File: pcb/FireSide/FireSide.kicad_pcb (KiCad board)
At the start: 2 copper layers, 120 x 80 mm, 27 parts, among them J0 SDIOModule, J1 D4184_PIN_A, J10 5V_01x02_JST, J11 5V_01x02_JST, J12 Status_01x02_JST, J2 D4184_PIN_B, J3 D4184_PIN_C, J4 A0_01x02_JST, J5 A1_01x02_JST, J6 A2_01x02_JST, J60 XT60-Male, J7 A3_01x02_JST, J8 A4_01x02_JST, J9 A5_01x02_JST, Q1 MMBT2222A, U1 AMS1117-5.0, U3 RYLR998

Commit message: [FS] PCB Updated to v1.1.6
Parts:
- removed A1: Nucleo-L412KB, Module:Arduino_Nano
- removed H5, H6: BoardM4, MountingHole:MountingHole_4.3mm_M4_ISO7380_Pad_TopBottom
- removed J0: SDIOModule, Connector_Molex:Molex_Nano-Fit_105309-xx08_1x08_P2.50mm_Vertical
- removed J60: XT60-Male, XT60-M:AMASS_XT60-M
- removed R1: 1k, Resistor_SMD:R_0805_2012Metric_Pad1.20x1.40mm_HandSolder
- added C3: 10uF, Capacitor_SMD:C_0805_2012Metric, F.Cu at (107.0, 46.8)
- added C4: 22uF, Capacitor_SMD:C_0805_2012Metric, F.Cu at (90.8, 50.5)
- added C5: 100nF, Capacitor_SMD:C_0805_2012Metric, F.Cu at (130.9, 67.6)
- added C6: 4.7uF, Capacitor_SMD:C_0805_2012Metric, F.Cu at (130.9, 71.0)
- added G***: LOGO, logos:logo2, F.Cu at (106.1, 64.4)
- added J13: Screw_Terminal_01x03, TerminalBlock:TerminalBlock_bornier-3_P5.08mm, F.Cu at (139.8, 52.9)
- added J14: Conn_01x02_Pin, Connector_JST:JST_XH_B2B-XH-A_1x02_P2.50mm_Vertical, F.Cu at (142.8, 65.2)
- added R2: 100k, Resistor_THT:R_Axial_DIN0204_L3.6mm_D1.6mm_P5.08mm_Horizontal, F.Cu at (147.8, 109.5)
- added R4: 1k, Resistor_SMD:R_0805_2012Metric, F.Cu at (128.2, 54.0)
- added R5: 100k, Resistor_THT:R_Axial_DIN0204_L3.6mm_D1.6mm_P5.08mm_Horizontal, F.Cu at (147.8, 96.5)
- added R6: 100k, Resistor_THT:R_Axial_DIN0204_L3.6mm_D1.6mm_P5.08mm_Horizontal, F.Cu at (147.8, 83.5)
- added R7: 100k, Resistor_THT:R_Axial_DIN0204_L3.6mm_D1.6mm_P5.08mm_Horizontal, F.Cu at (147.8, 70.5)
- added TP1: TestPoint, TestPoint:TestPoint_Loop_D2.60mm_Drill1.6mm_Beaded, F.Cu at (126.5, 48.5)
- added TP2: TestPoint, TestPoint:TestPoint_Loop_D2.60mm_Drill1.6mm_Beaded, F.Cu at (95.2, 42.2)
- added U2: ~, FireSide Footprint:RYLR998, F.Cu at (78.7, 67.3)
- added U4: AMS1117-5.0, Package_TO_SOT_SMD:SOT-223-3_TabPin2, F.Cu at (113.0, 50.9)
- added U5: ~, FireSide Footprint:D4184, F.Cu at (95.0, 85.8)
- added U6: ~, FireSide Footprint:D4184, F.Cu at (95.0, 121.0)
- added U8: ~, FireSide Footprint:XT60-M, F.Cu at (107.6, 29.6)
- added U9: ~, FireSide Footprint:D4184, F.Cu at (95.0, 103.2)
- C1: value 22u -> 22uF; footprint Capacitor_THT:CP_Radial_D5.0mm_P2.50mm -> Capacitor_SMD:C_0805_2012Metric
- C2: value 22u -> 10uF; footprint Capacitor_THT:CP_Radial_D5.0mm_P2.50mm -> Capacitor_SMD:C_0805_2012Metric
- H1, H2: value SDModuleM3 -> MountingHole_Pad; footprint MountingHole:MountingHole_3.2mm_M3_ISO7380_Pad_TopBottom -> MountingHole:MountingHole_4.3mm_M4_DIN965_Pad
- H3, H4: value BoardM4 -> MountingHole_Pad; footprint MountingHole:MountingHole_4.3mm_M4_ISO7380_Pad_TopBottom -> MountingHole:MountingHole_4.3mm_M4_DIN965_Pad
- J1: value D4184_PIN_A -> Conn_01x02_Pin; footprint Connector_JST:JST_XH_B4B-XH-A_1x04_P2.50mm_Vertical -> Connector_JST:JST_XH_B2B-XH-A_1x02_P2.50mm_Vertical
- J10, J11: value 5V_01x02_JST -> Conn_01x02_Pin
- J12: value Status_01x02_JST -> Conn_01x02_Pin
- J2: value D4184_PIN_B -> Conn_01x02_Pin; footprint Connector_JST:JST_XH_B4B-XH-A_1x04_P2.50mm_Vertical -> Connector_JST:JST_XH_B2B-XH-A_1x02_P2.50mm_Vertical
- J3: value D4184_PIN_C -> Conn_01x08_Pin; footprint Connector_JST:JST_XH_B4B-XH-A_1x04_P2.50mm_Vertical -> Connector_PinHeader_2.54mm:PinHeader_1x08_P2.54mm_Vertical
- J4: value A0_01x02_JST -> Conn_01x02_Pin
- J5: value A1_01x02_JST -> Conn_01x02_Pin
- J6: value A2_01x02_JST -> Conn_01x02_Pin
- J7: value A3_01x02_JST -> Conn_01x02_Pin
- J8: value A4_01x02_JST -> Conn_01x02_Pin
- J9: value A5_01x02_JST -> Screw_Terminal_01x03; footprint Connector_JST:JST_XH_B2B-XH-A_1x02_P2.50mm_Vertical -> TerminalBlock:TerminalBlock_bornier-3_P5.08mm
- Q1: moved to F.Cu
- U1: value AMS1117-5.0 -> AMS1117-3.3; moved to F.Cu
- U3: value RYLR998 -> NUCLEO-L412KB; footprint RYLR998:RYLR998 -> FireSide Footprint:NUCLEO-L412KB
- moved H1 141.4 mm to (149.0, 145.6), turned to 90 degrees
- moved J3 118.0 mm to (130.6, 124.5), turned to -90 degrees
- moved J2 111.0 mm to (142.2, 115.2), turned to 0 degrees
- moved J1 109.1 mm to (142.2, 123.5), turned to 0 degrees
- moved H4 108.3 mm to (149.0, 34.5), turned to 90 degrees
- moved H2 79.3 mm to (76.5, 145.6), turned to 90 degrees
- moved J9 77.3 mm to (81.8, 44.2), turned to -90 degrees
- moved H3 72.9 mm to (76.5, 34.5), turned to 90 degrees
- moved J11 64.3 mm to (85.8, 34.0)
- moved J4 60.7 mm to (142.8, 104.2), turned to 90 degrees
- moved J7 58.0 mm to (122.8, 35.8), turned to -90 degrees
- moved J8 57.7 mm to (130.5, 35.8), turned to -90 degrees
- moved J5 48.3 mm to (142.8, 91.2), turned to 90 degrees
- moved J6 39.8 mm to (142.8, 78.2), turned to 90 degrees
- moved U1 35.3 mm to (97.8, 50.5), turned to 180 degrees
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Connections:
- C1 pad 1: +BATT -> 5V
- C2 pad 1: /5VIN -> VI
- J1 pad 1: /FIRE_PIN_A -> A0
- J10 pad 1: /5VIN -> Net-(J10-Pin_1)
- J10 pad 2: GND -> VI
- J11 pad 1: /5VIN -> GND
- J11 pad 2: GND -> 3.3V
- J12 pad 1: +BATT -> GND
- J12 pad 2: Net-(J12-Pin_2) -> 3.3V
- J2 pad 1: /FIRE_PIN_B -> A1
- J3 pad 1: /FIRE_PIN_C -> 3.3V_STM
- J3 pad 3: GND -> SCK_SD
- J3 pad 4: +BATT -> MISO_SD
- J4 pad 1: Net-(A1-A0) -> A_THERM-1
- J5 pad 1: Net-(A1-A1) -> A_THERM-2
- J6 pad 1: Net-(A1-A2) -> A_THERM-3
- J7 pad 1: Net-(A1-A3) -> GND
- J7 pad 2: GND -> 5V
- J8 pad 1: Net-(A1-SDA/A4) -> GND
- J8 pad 2: GND -> 5V
- J9 pad 1: Net-(A1-SCL/A5) -> 3.3V
- Q1 pad 1: /STATUS_PIN -> STATUS_PIN
- U1 pad 2: /5VIN -> 3.3V
- U1 pad 3: +BATT -> VI
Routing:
- net 3.3V_STM: track 0.00 -> 125.6 mm
- net Net-(A1-3V3): track 120.4 -> 0.00 mm, vias 3 -> 0
- net /5VIN: track 103.6 -> 0.00 mm, vias 2 -> 0
- net +BATT: track 82.6 -> 0.00 mm
- net /FIRE_PIN_C: track 60.8 -> 0.00 mm
- net /FIRE_PIN_B: track 56.3 -> 0.00 mm
- net 5V: track 0.00 -> 53.0 mm
- net VI: track 0.00 -> 50.8 mm
- net /FIRE_PIN_A: track 50.5 -> 0.00 mm
- net 3.3V: track 0.00 -> 46.0 mm
- net Net-(A1-SCK): track 44.5 -> 0.00 mm, vias 2 -> 0
- net Net-(A1-D10): track 42.8 -> 0.00 mm
- net A_THERM-4: track 0.00 -> 41.1 mm
- net Net-(A1-RX1): track 40.8 -> 0.00 mm
- net STATUS_PIN: track 0.00 -> 40.4 mm
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- removed copper zone on F.Cu, net GND
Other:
- board size 120 x 80 mm -> 84 x 122 mm
- board text added: "-------------- SANYUKTA DUTTA TEJASWINEE GUNJAL KRISHNA GUND MYTREYA BADAMPUDI YASH PATIDAR RISHIT KULKARNI DEEPSHIKHA SARANGI --------------"
- board text added: "10uF"
- board text added: "22uF"
- board text added: "3.3V"
- board text added: "3.3V CHANNELS"
- board text added: "3.3Vin"
- board text added: "3V3"
- board text added: "5V"
- board text added: "5V CHANNELS"
- board text added: "5Vin"
- board text added: "7.4V"
- board text added: "A0"
- board text added: "A1"
- board text added: "AMS1117 3.3V"
- board text added: "AMS1117 5V"
- board text added: "ANALOG CHANNELS"
- board text added: "CLK"
- board text added: "CMD"
- board text added: "D0"
- board text added: "D0-TX_RYLR D1-RX_RYLR D2-LAUNCH_LED D4-ARM_LED D3-D4184(1) D6-D4184(2) D9-D4184(3) D5-STATUS D10-CS D11-MOSI D12-MISO D13-SCK A0:A1-ANALOG A2:A5-THERM"
- board text added: "D1"
- board text added: "D2"
- board text added: "D3"
- board text added: "D4184 (1)"
- board text added: "D4184 (2)"
- board text added: "D4184 (3)"
- board text added: "FireSide"
- board text added: "GND"
- board text added: "MCU SWITCH"
- board text added: "NUCLEO-L412KB"
- board text added: "RYLR SWITCH"
- board text added: "SD CARD MODULE"
- board text added: "STATUS INDICATOR"
- board text added: "T1"
- board text added: "T2"
- board text added: "T3"
- board text added: "T4"
- board text added: "THERMISTOR (1)"
- board text added: "THERMISTOR (2)"
- board text added: "THERMISTOR (3)"
- board text added: "THERMISTOR (4)"
- board text added: "TP 3.3V"
- board text added: "TP 5V"
- board text added: "are you sure??"
- board text added: "special thanks to bunty"
- board text removed: "TMIT FireSide"

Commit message: [FS] Updated FireSide PCB with RYLR993
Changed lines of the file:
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@@
 		)
 		(fp_rect
-			(start -1.66 -20.99)
-			(end -7.22 -4.72)
-			(stroke
-				(width 0.1)
-				(type default)
-			)
-			(fill no)
-			(layer "F.SilkS")
-		)
-		(fp_rect
 			(start 6.9 -4.77)
 			(end -7.25 10.05)
@@
 		)
 		(fp_rect
-			(start -1.66 -4.72)
-			(end -7.16 -20.92)
-			(stroke
-				(width 0.1)
-				(type default)
-			)
-			(fill no)
-			(layer "F.Fab")
-		)
-		(fp_rect
 			(start 6.59 -4.42)
 			(end -3.61 7.08)
@@
 		)
 		(embedded_fonts no)
-		(model "${KIPRJMOD}/FireSide step files/RYLR998.stp"
+		(model "C:/Users/TEJASWINEE/Downloads/RYLR993_Lite_3D/RYLR993_Lite_3D/RYLR993_Lite.stp"
 			(offset
-				(xyz 57 -8 3)
+				(xyz 7.5 -7 2)
 			)
 			(scale
@@
 			)
 			(rotate
-				(xyz -0 180 -0)
+				(xyz -180 -0 -180)
 			)
 		)
@@
 	)
 	(zone
-		(net 10)
-		(net_name "RX_RYLR")
-		(layer "F.Cu")
-		(name "$teardrop_padvia$")
-		(hatch none 0.1)
-		(priority 30031)
-		(attr
-			(teardrop
-				(type padvia)
-			)
-		)
-		(connect_pads yes
-			(clearance 0)
-		)
-		(min_thickness 0.0254)
-		(filled_areas_thickness no)
-		(fill yes
-			(thermal_gap 0.5)
-			(thermal_bridge_width 0.5)
-			(island_removal_mode 1)
-			(island_area_min 10)
-		)
-		(polygon
-			(pts
-				(xy 89.532667 66.85) (xy 89.532667 66.65) (xy 88.321235 66.043251) (xy 87.848 66.75) (xy 88.321235 67.456749)
-			)
-		)
-	)
-	(zone
 		(net 16)
 		(net_name "PWM_D4184-3")
@@
 	)
 	(zone
-		(net 23)
-		(net_name "5Vin")
+		(net 10)
+		(net_name "RX_RYLR")
 		(layer "F.Cu")
 		(name "$teardrop_padvia$")
 		(hatch none 0.1)
-		(priority 30013)
+		(priority 30001)
 		(attr
 			(teardrop
@@
 		(polygon
 			(pts
-				(xy 130.389181 73.990642) (xy 129.589181 73.990642) (xy 129.242642 75.351341) (xy 129.99 75.501)
-				(xy 130.737358 75.351341)
+				(xy 89.532667 66.85) (xy 89.532667 66.65) (xy 88.321235 66.043251) (xy 87.848 66.75) (xy 88.321235 67.456749)
 			)
 		)
 	)
 	(zone
-		(net 15)
-		(net_name "PWM_D4184-1")
+		(net 23)
+		(net_name "5Vin")
 		(layer "F.Cu")
 		(name "$teardrop_padvia$")
 		(hatch none 0.1)
-		(priority 30024)
+		(priority 30013)
 		(attr
 			(teardrop
@@
 		(polygon
 			(pts
-				(xy 105.782707 83.35) (xy 105.782707 83.15) (xy 104.500013 82.501677) (xy 103.999 83.25) (xy 104.500013 83.998323)
+				(xy 130.389181 73.990642) (xy 129.589181 73.990642) (xy 129.242642 75.351341) (xy 129.99 75.501)
+				(xy 130.737358 75.351341)
 			)
 		)
 	)
 	(zone
-		(net 27)
-		(net_name "3.3Vin")
+		(net 15)
+		(net_name "PWM_D4184-1")
 		(layer "F.Cu")
 		(name "$teardrop_padvia$")
 		(hatch none 0.1)
-		(priority 30009)
+		(priority 30024)
 		(attr
 			(teardrop
@@
 		(polygon
 			(pts
-				(xy 86.165333 61.27) (xy 86.165333 62.07) (xy 87.683173 62.503667) (xy 87.85 61.67) (xy 87.683173 60.836333)
+				(xy 105.782707 83.35) (xy 105.782707 83.15) (xy 104.500013 82.501677) (xy 103.999 83.25) (xy 104.500013 83.998323)
 			)
 		)
@@
 		(name "$teardrop_padvia$")
 		(hatch none 0.1)
-		(priority 30032)
+		(priority 30002)
 		(attr
 			(teardrop
@@
 			)
 		)
+	)
+	(zone
+		(net 27)
+		(net_name "3.3Vin")
+		(layer "F.Cu")
+		(name "$teardrop_padvia$")
+		(hatch none 0.1)
+		(priority 30000)
+		(attr
+			(teardrop
+				(type padvia)
+			)
+		)
+		(connect_pads yes
+			(clearance 0)
+		)
+		(min_thickness 0.0254)
+		(filled_areas_thickness no)
+		(fill yes
+			(thermal_gap 0.5)
+			(thermal_bridge_width 0.5)
+			(island_removal_mode 1)
+			(island_area_min 10)
+		)
+		(polygon
+			(pts
+				(xy 86.165333 61.27) (xy 86.165333 62.07) (xy 87.683173 62.503667) (xy 87.85 61.67) (xy 87.683173 60.836333)
+			)
+		)

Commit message: [FS] Updated PCB (v1.2.0)
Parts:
- removed C1: 22uF, Capacitor_SMD:C_0805_2012Metric
- removed C2: 10uF, Capacitor_SMD:C_0805_2012Metric
- removed U4: AMS1117-5.0, Package_TO_SOT_SMD:SOT-223-3_TabPin2
- added C7: 0.1uF, Capacitor_SMD:C_0805_2012Metric, F.Cu at (99.8, 44.8)
- added C8: 22uF, Capacitor_SMD:C_0805_2012Metric, F.Cu at (112.2, 44.5)
- added R1: 1M, Resistor_THT:R_Axial_DIN0204_L3.6mm_D1.6mm_P5.08mm_Horizontal, F.Cu at (148.2, 125.4)
- added R3: 1M, Resistor_THT:R_Axial_DIN0204_L3.6mm_D1.6mm_P5.08mm_Horizontal, F.Cu at (148.2, 114.7)
- added U7: MIC5209-3.3YS, MIC5209-3.3YS-Microchip-Symbol-Kicad-237169:SOT-223-3, F.Cu at (97.8, 53.6)
- C3: value 10uF -> 0.1uF
- U1: value AMS1117-3.3 -> MIC5209-5YS; footprint Package_TO_SOT_SMD:SOT-223-3_TabPin2 -> MIC5209-5.0YS-TR:SOT230P700X180-4N
- moved U1 15.4 mm to (113.1, 50.0), turned to 0 degrees
- moved J1 4.41 mm to (142.0, 127.9), turned to 90 degrees
- moved J2 1.96 mm to (142.1, 117.2), turned to 90 degrees
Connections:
- J1 pad 1: A0 -> GND
- J1 pad 2: GND -> A0
- J2 pad 1: A1 -> GND
- J2 pad 2: GND -> A1
- U1 pad 1: GND -> VI
- U1 pad 2: 3.3V -> GND
- U1 pad 3: VI -> 5V
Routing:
- net 5V: track 53.0 -> 62.5 mm
- net A0: track 28.5 -> 37.7 mm
- net 3.3V_STM: track 125.6 -> 132.5 mm
- net A1: track 22.3 -> 28.5 mm
- net GND: track 14.3 -> 17.1 mm
- net VI: track 50.8 -> 53.1 mm
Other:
- board text added: "MIC5209 3.3V"
- board text added: "MIC5209-5.0YS"
- board text removed: "AMS1117 3.3V"
- board text removed: "AMS1117 5V"

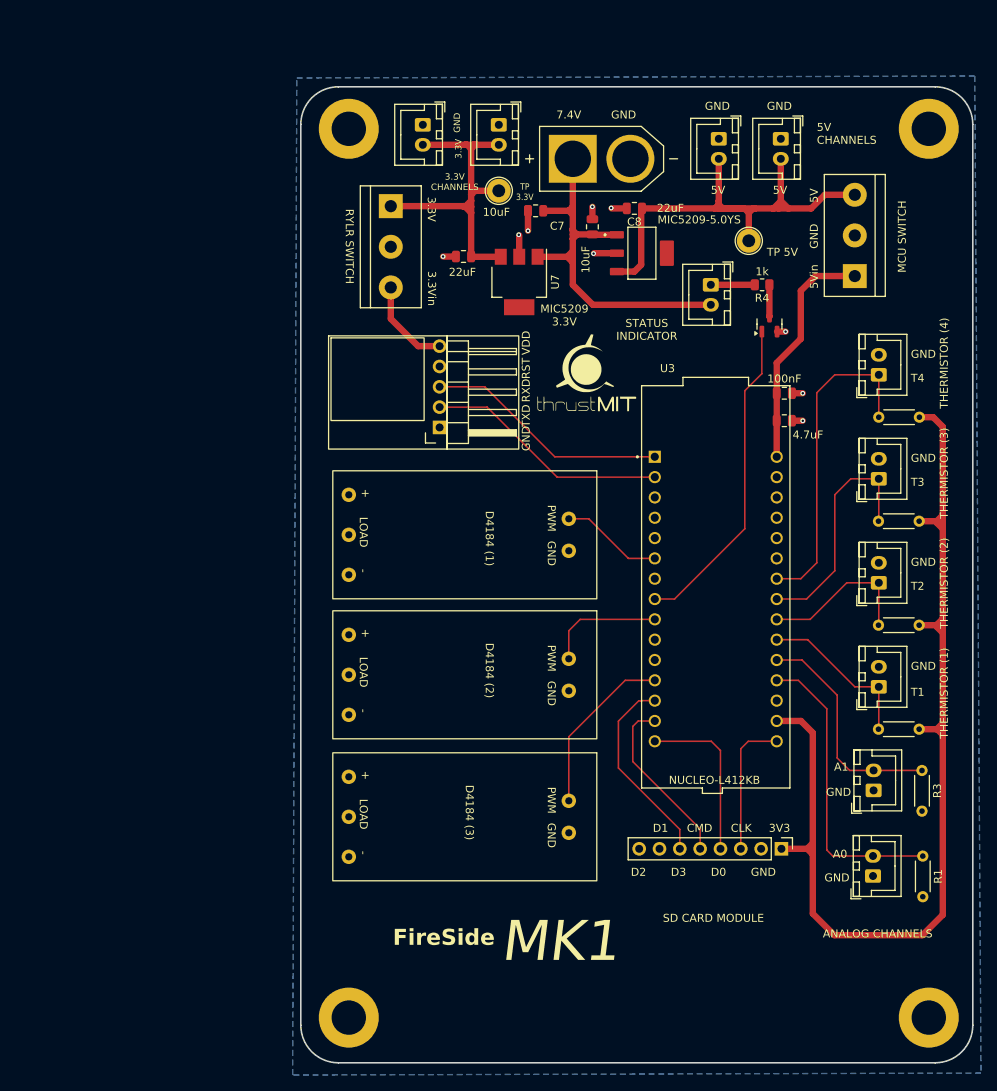
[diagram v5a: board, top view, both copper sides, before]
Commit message: [FS] Remove AMS1117 Regulators & Apply ECSS-E-ST-20-21C Standard
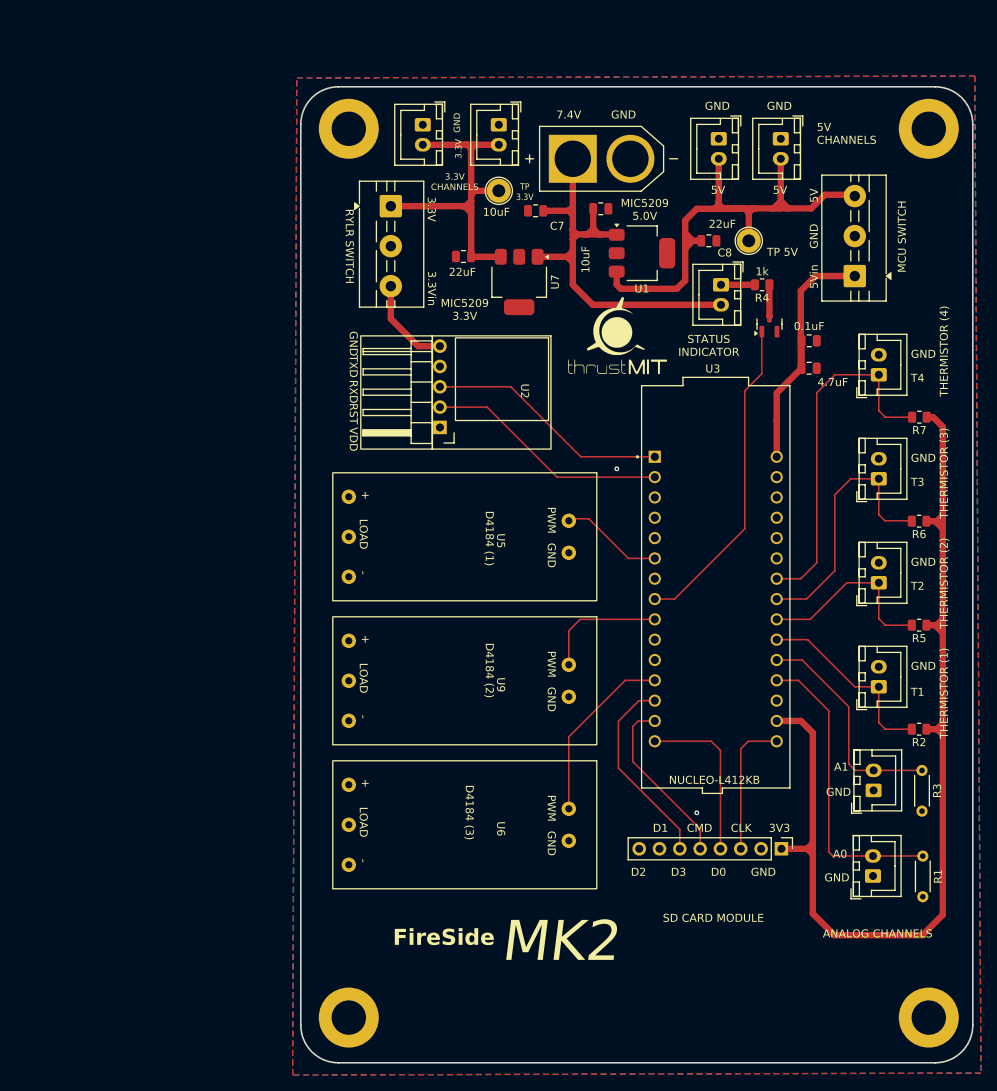
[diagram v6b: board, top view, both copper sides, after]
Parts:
- C5: value 100nF -> 0.1uF
- J13, J9: footprint TerminalBlock:TerminalBlock_bornier-3_P5.08mm -> TerminalBlock:TerminalBlock_MaiXu_MX126-5.0-03P_1x03_P5.00mm
- L0: renamed from G***; value LOGO -> TMIT; footprint logos:logo2 -> FireSide Footprint:TMIT-Logo
- R2, R5, R6, R7: value 100k -> 100k +/- 0.1%; footprint Resistor_THT:R_Axial_DIN0204_L3.6mm_D1.6mm_P5.08mm_Horizontal -> Resistor_SMD:R_0805_2012Metric
- U1: footprint MIC5209-5.0YS-TR:SOT230P700X180-4N -> Package_TO_SOT_SMD:SOT-223-3_TabPin2
- U2: footprint FireSide Footprint:RYLR998 -> FireSide Footprint:RYLR993
- U7: footprint MIC5209-3.3YS-Microchip-Symbol-Kicad-237169:SOT-223-3 -> Package_TO_SOT_SMD:SOT-223-3_TabPin2
- moved U2 18.3 mm to (97.0, 67.3), turned to -90 degrees
- moved C8 10.1 mm to (121.5, 48.5), turned to 0 degrees
- moved C5 7.26 mm to (134.1, 61.0)
- moved C6 7.26 mm to (134.0, 64.4)
- moved L0 6.03 mm to (110.0, 59.8)
- moved C3 2.48 mm to (108.0, 44.5), turned to 0 degrees
- moved J10 1.28 mm to (123.0, 54.0)
- moved U6 1.00 mm to (95.0, 122.0)
- moved U9 0.75 mm to (95.0, 104.0)
- moved U5 0.25 mm to (95.0, 86.0)
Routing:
- net GND: track 17.1 -> 0.00 mm, vias 9 -> 2
- net 5V: track 62.5 -> 70.4 mm
- net VI: track 53.1 -> 60.5 mm
- net A_THERM-4: track 41.1 -> 44.8 mm
- net 3.3V_STM: track 132.5 -> 128.8 mm
- net A_THERM-2: track 20.0 -> 23.6 mm
- net A_THERM-1: track 20.5 -> 24.2 mm
- net A_THERM-3: track 29.9 -> 33.5 mm
- net 5Vin: track 29.5 -> 32.9 mm
- net Net-(J10-Pin_1): track 5.50 -> 4.22 mm
- net PWM_D4184-3: track 21.7 -> 22.7 mm
- added copper zone on F.Cu, net GND
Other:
- board text added: "MIC5209 5.0V"
- board text added: "MK2"
- board text removed: "MIC5209-5.0YS"
- board text removed: "MK1"
- board text removed: "are you sure??"
